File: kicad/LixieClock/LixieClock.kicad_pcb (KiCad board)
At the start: 2 copper layers, 21 parts, among them Q1 Q_PNP_ECB, Q2 Q_PNP_ECB, Q3 Q_PNP_ECB, Q4 Q_PNP_ECB, Q5 Q_PNP_ECB, Q6 Q_PNP_ECB, SW1 Rotary_Encoder, SW2 SW_Push, U1 2DigitLixie, U2 2DigitLixie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

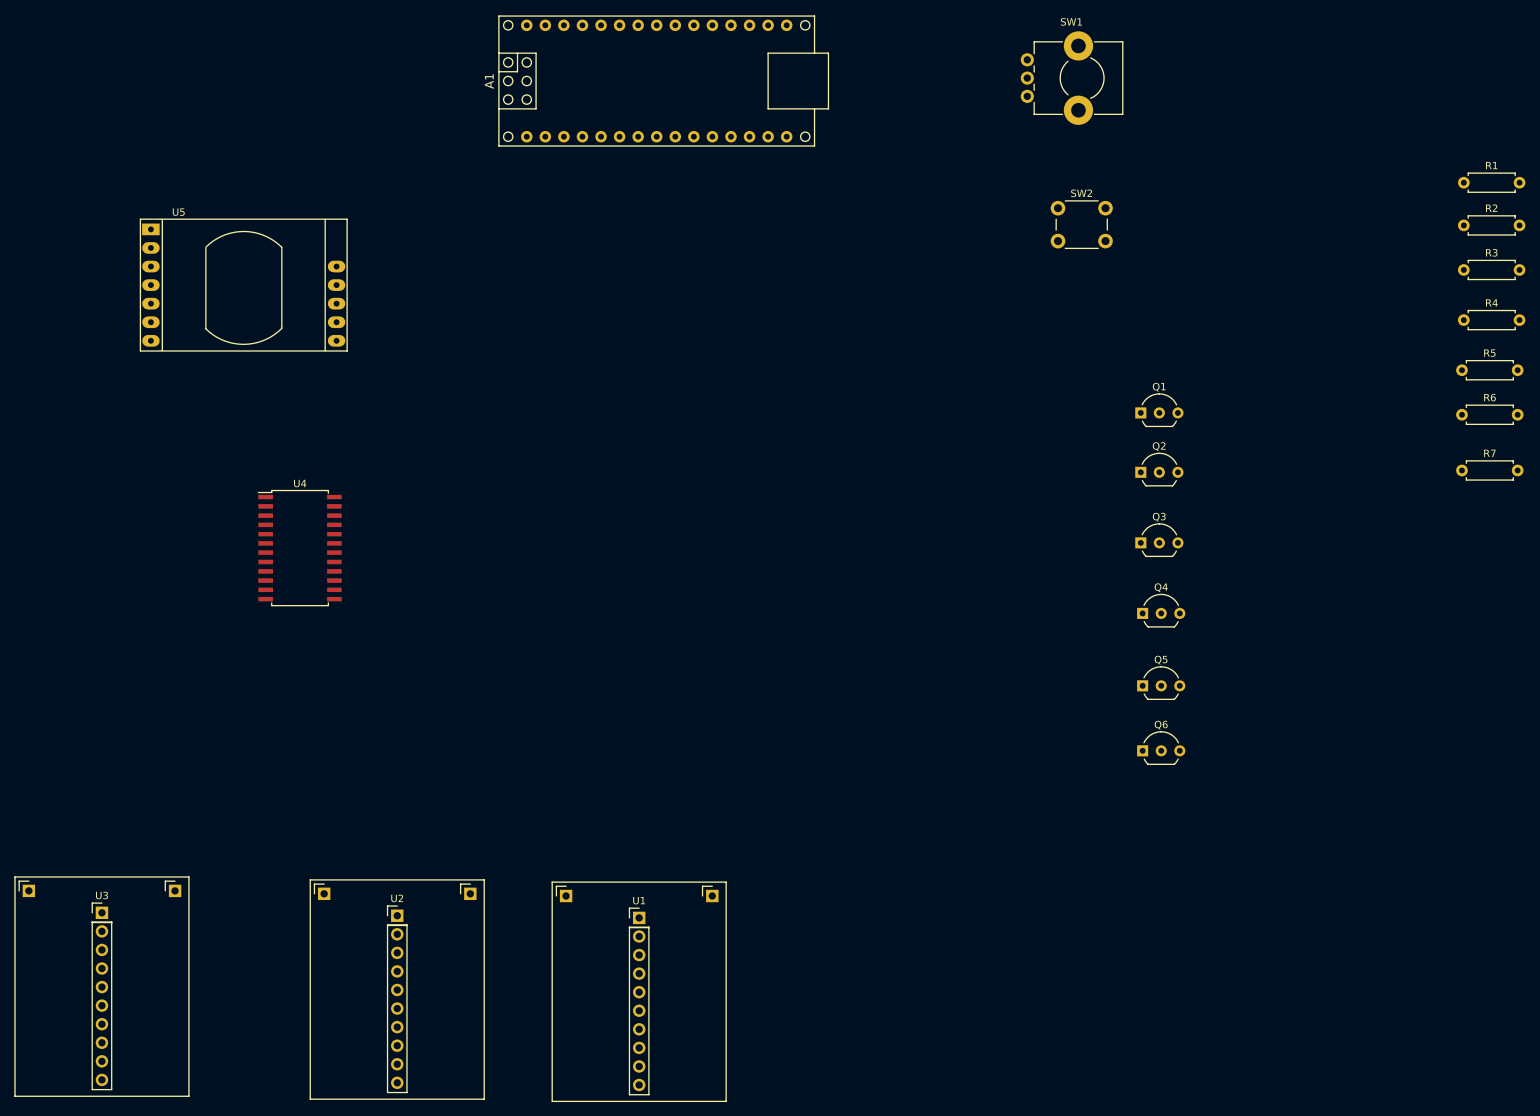
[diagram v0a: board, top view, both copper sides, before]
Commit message: 100×100mmのサイズに収めるにはちょっと無理があったので、LixieUnit <-> Mounter <-> MainBoardという3層構造に変更した。
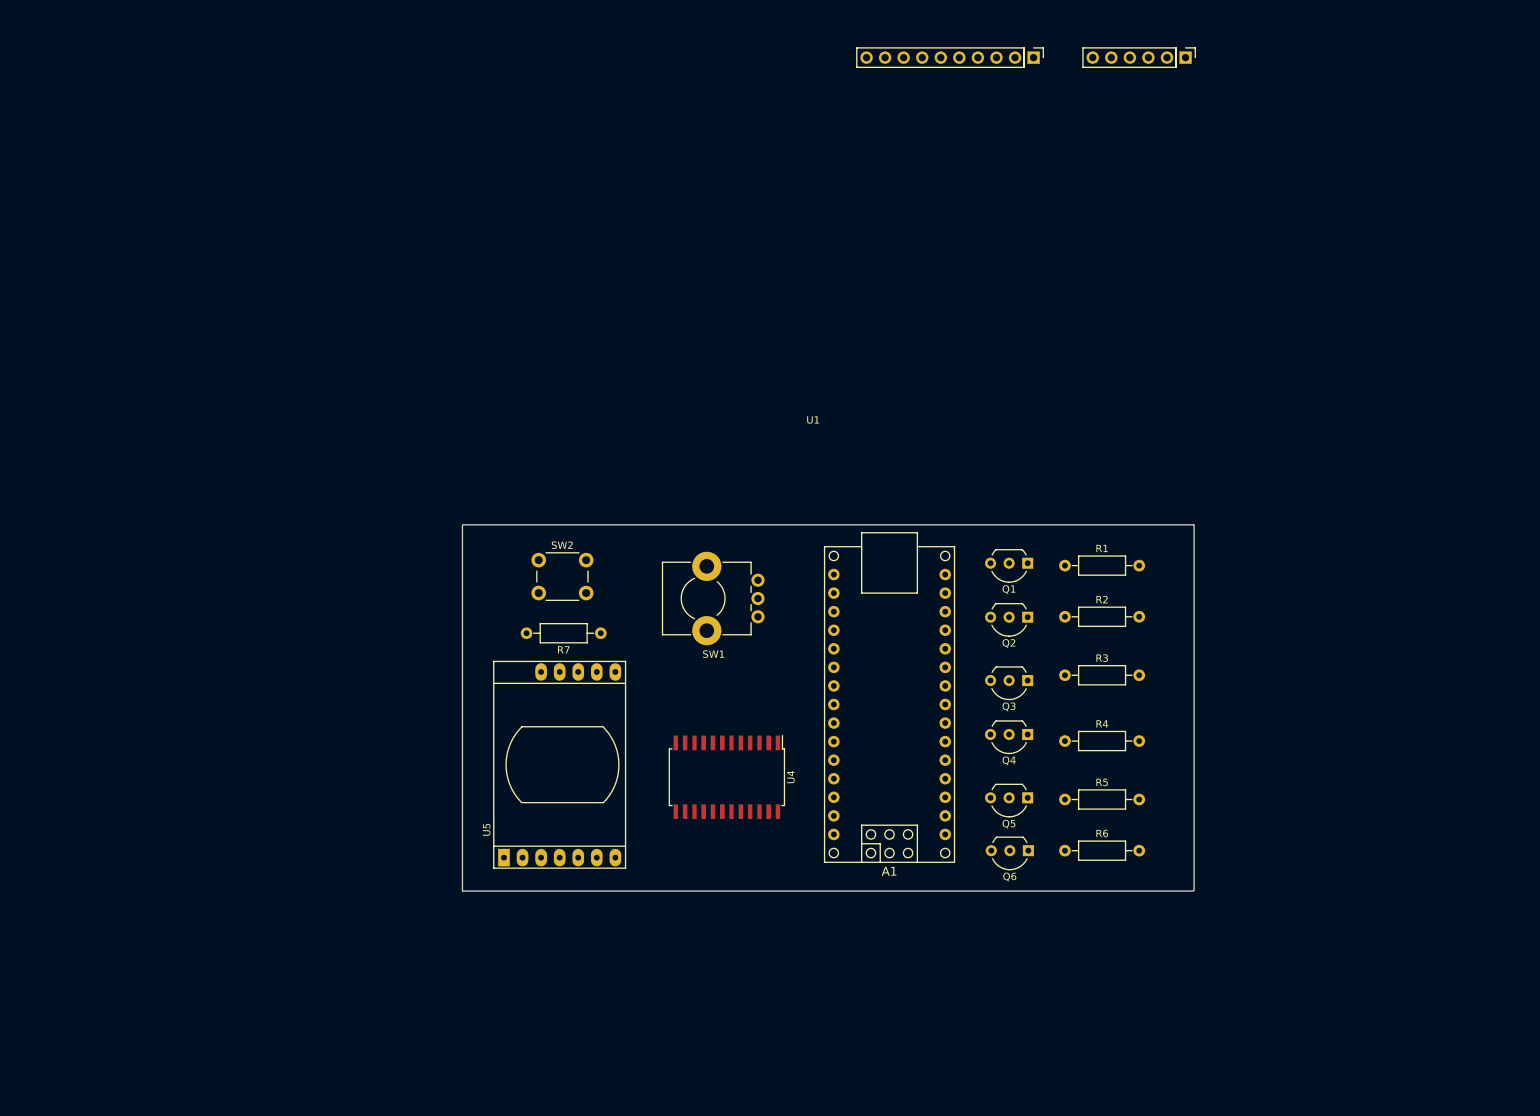
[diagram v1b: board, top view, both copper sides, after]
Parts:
- removed U2, U3: 2DigitLixie, LixieClock:LixieUnit
- R1, R2, R3, R4, R5, R6, R7: footprint Resistors_THT:R_Axial_DIN0207_L6.3mm_D2.5mm_P7.62mm_Horizontal -> Resistors_THT:R_Axial_DIN0207_L6.3mm_D2.5mm_P10.16mm_Horizontal
- U1: value 2DigitLixie -> 6DigitLixie; footprint LixieClock:LixieUnit -> LixieClock:6DigitLixie
- moved R7 119.9 mm to (124.8, 119.5), turned to 180 degrees
- moved U5 98.6 mm to (111.5, 150.2), turned to 90 degrees
- moved A1 91.1 mm to (164.2, 129.3), turned to 90 degrees
- moved SW2 85.8 mm to (116.2, 109.5)
- moved R6 80.7 mm to (188.2, 149.3)
- moved R5 80.0 mm to (188.2, 142.3)
- moved R4 79.3 mm to (188.2, 134.3)
- moved R3 77.8 mm to (188.2, 125.3)
- moved R2 76.5 mm to (188.2, 117.3)
- moved SW1 75.8 mm to (146.2, 112.3), turned to 180 degrees
- moved R1 75.6 mm to (188.2, 110.3)
- moved U1 74.6 mm to (107.5, 87.9)
- moved U4 66.3 mm to (142.0, 139.2), turned to 270 degrees
- moved Q1 25.7 mm to (183.2, 110.0), turned to 180 degrees
- moved Q2 25.1 mm to (183.2, 117.4), turned to 180 degrees
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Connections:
- U1 pad 1: Net-(Q2-Pad1) -> Net-(Q6-Pad1)
- U1 pad 2: Net-(Q1-Pad1) -> Net-(Q5-Pad1)
- U1 pad 3: Net-(U1-Pad3) -> Net-(Q4-Pad1)
- U1 pad 4: Net-(U1-Pad4) -> Net-(Q3-Pad1)
- U1 pad 5: Net-(U1-Pad5) -> Net-(Q2-Pad1)
- U1 pad 6: Net-(U1-Pad6) -> Net-(Q1-Pad1)
- U4 pad 1: Net-(U1-Pad3) -> Net-(U1-Pad7)
- U4 pad 10: Net-(U1-Pad12) -> Net-(U1-Pad16)
- U4 pad 2: Net-(U1-Pad4) -> Net-(U1-Pad8)
- U4 pad 3: Net-(U1-Pad5) -> Net-(U1-Pad9)
- U4 pad 4: Net-(U1-Pad6) -> Net-(U1-Pad10)
- U4 pad 5: Net-(U1-Pad7) -> Net-(U1-Pad11)
- U4 pad 6: Net-(U1-Pad8) -> Net-(U1-Pad12)
- U4 pad 7: Net-(U1-Pad9) -> Net-(U1-Pad13)
- U4 pad 8: Net-(U1-Pad10) -> Net-(U1-Pad14)
- U4 pad 9: Net-(U1-Pad11) -> Net-(U1-Pad15)
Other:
- board outline added: 100.1 x 50.1 mm

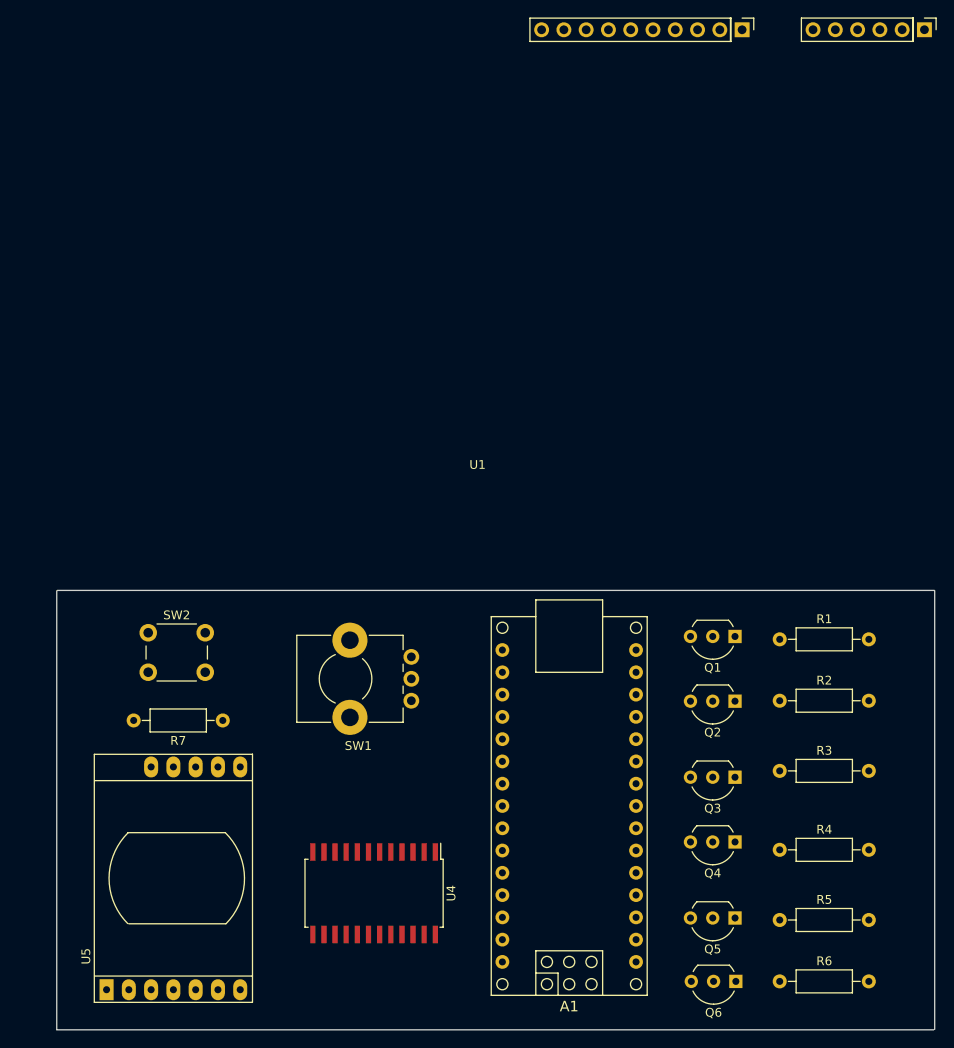
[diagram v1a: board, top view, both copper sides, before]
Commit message: 自動配線後、手作業で引き直し中
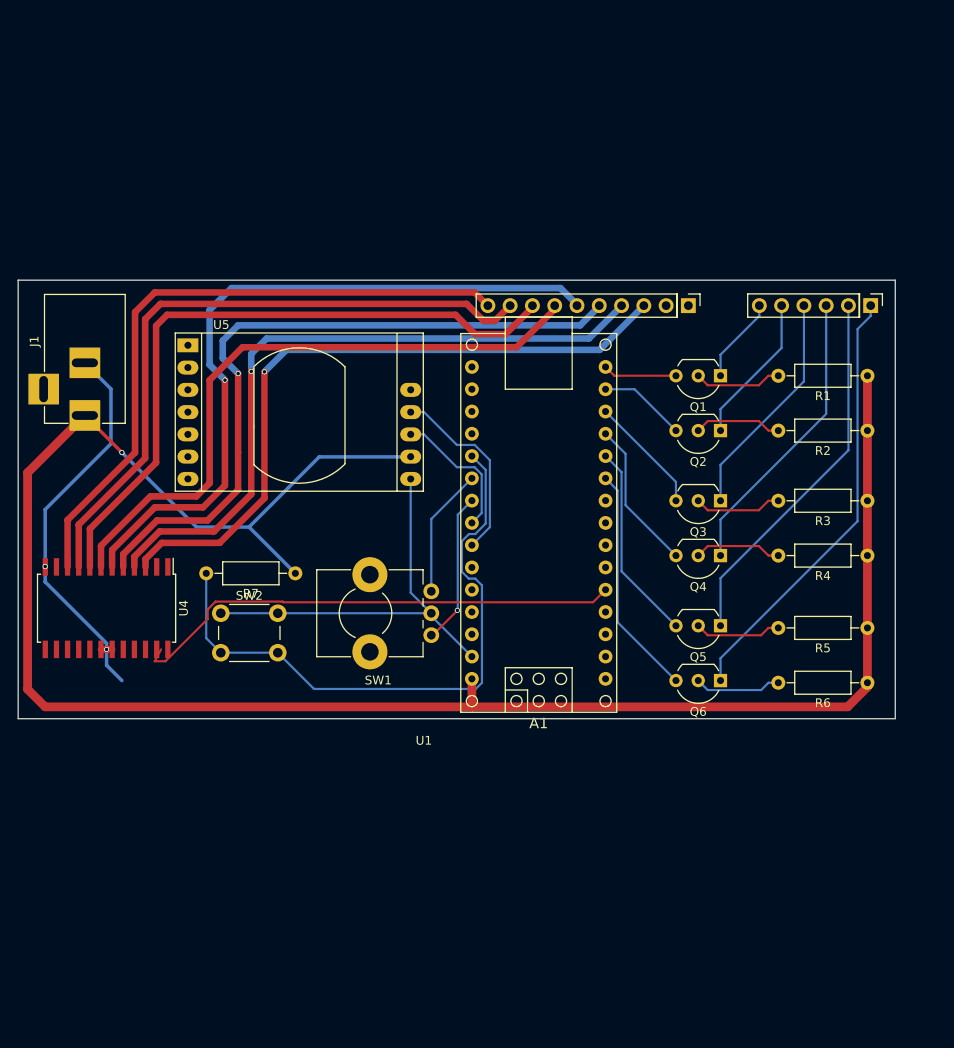
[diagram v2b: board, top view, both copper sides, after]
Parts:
- added J1: Jack-DC, Connectors:BARREL_JACK, F.Cu at (109.0, 84.8)
- moved U5 74.1 mm to (120.8, 76.8), turned to 0 degrees
- moved U4 44.6 mm to (111.5, 106.8)
- moved R6 35.5 mm to (198.2, 115.2), turned to 180 degrees
- moved R4 35.0 mm to (198.2, 100.8), turned to 180 degrees
- moved R5 34.8 mm to (198.2, 109.0), turned to 180 degrees
- moved Q6 34.3 mm to (181.5, 115.0)
- moved Q5 33.4 mm to (181.5, 108.8)
- moved Q4 32.7 mm to (181.5, 100.8)
- moved A1 32.5 mm to (160.8, 97.0)
- moved R2 32.4 mm to (198.2, 86.5), turned to 180 degrees
- moved R3 32.4 mm to (198.2, 94.5), turned to 180 degrees
- moved U1 32.0 mm to (101.4, 119.3)
- moved R1 31.7 mm to (198.2, 80.2), turned to 180 degrees
- moved Q3 31.6 mm to (181.5, 94.5)
- moved Q2 30.9 mm to (181.5, 86.5)
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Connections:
- net +5V renamed 5V
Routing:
- net 5V: track 0.00 -> 223.4 mm, vias 0 -> 1
- net GND: track 0.00 -> 93.0 mm, vias 0 -> 2
- net Net-(U1-Pad12): track 0.00 -> 82.8 mm, vias 0 -> 1
- net Net-(U1-Pad11): track 0.00 -> 79.9 mm, vias 0 -> 1
- net Net-(U1-Pad9): track 0.00 -> 78.1 mm, vias 0 -> 1
- net Net-(U1-Pad10): track 0.00 -> 78.0 mm, vias 0 -> 1
- net Net-(U1-Pad14): track 0.00 -> 76.4 mm
- net Net-(U1-Pad15): track 0.00 -> 75.3 mm
- net Net-(U1-Pad16): track 0.00 -> 74.0 mm
- net Net-(U1-Pad13): track 0.00 -> 72.6 mm
- net SW: track 0.00 -> 70.9 mm
- net A0: track 0.00 -> 57.0 mm
- net Net-(Q6-Pad1): track 0.00 -> 49.8 mm
- net Net-(Q5-Pad1): track 0.00 -> 42.5 mm
- net Net-(Q4-Pad1): track 0.00 -> 33.5 mm
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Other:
- board size 100.1 x 50.1 mm -> 100 x 50 mm
- net class Default: trace_width 0.25 -> 0.75

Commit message: 暫定的な基板の完成
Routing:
- net Net-(U1-Pad7): track 0.14 -> 108.5 mm, vias 0 -> 2
- net GND: track 93.0 -> 180.1 mm
- net Net-(U1-Pad8): track 0.00 -> 80.2 mm, vias 0 -> 1
- net A3: track 0.00 -> 67.3 mm, vias 0 -> 1
- net A2: track 0.00 -> 65.0 mm, vias 0 -> 1
- net A1: track 0.00 -> 60.8 mm, vias 0 -> 1
- net 5V: track 223.4 -> 242.2 mm
- net Net-(U1-Pad13): track 72.6 -> 77.7 mm
- net SW: track 70.9 -> 66.3 mm
- net Net-(U1-Pad12): track 82.8 -> 78.6 mm
- net Net-(U1-Pad11): track 79.9 -> 77.0 mm
- net A0: track 57.0 -> 59.1 mm, vias 0 -> 1
- net Net-(Q6-Pad2): track 9.93 -> 11.8 mm
- net DGT3: track 13.5 -> 15.3 mm
- net SCL: track 21.8 -> 23.6 mm
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- added copper zone on B.Cu, net GND
- added copper zone on F.Cu, net GND
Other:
- net class Default: trace_width 0.75 -> 0.25
